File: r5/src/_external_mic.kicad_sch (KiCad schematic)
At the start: 139 parts, among them Q12 BSS84PW, Q13 BSS84PW, Q14 NX6008NBKW, Q15 NX3008NBKW, Q16 NX3008NBKW, Q17 NX3008NBKW, Q18 NX3008NBKW, Q19 NX3008NBKW, Q20 BSS84PW, Q21 BSS84PW, Q22 NX3008NBKW, Q23 NX3008NBKW, Q24 NX3008NBKW, Q25 Si2323DS, Q29 Si2323DS, Q30 NX3008NBKW, T18 , T19 , T20 , T23 , T24 , T25 , T26 , T27 , T28 , T29 , T30 , T31 , T32 , T33 , T34 , T35 , T37 , T38 , T43 , T44 , T45 , T46 , T47 , T48 , T49 , T50 , T59 , U17 74HC20, U18 THAT5173, U19 74HC74, U20 74HC132, U21 74HC4520, U22 74HC132, U23 THAT1580, U24 74HC688, U25 LM4562, U26 74HC688, U27 AD4005, U36 APX809S-40SA

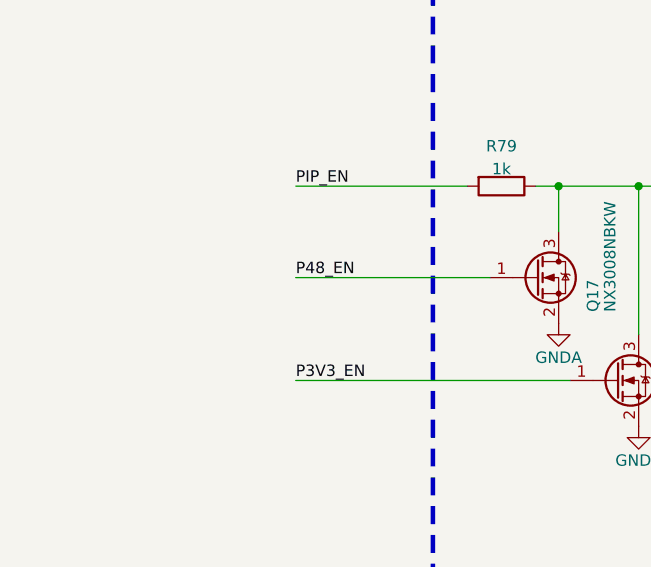
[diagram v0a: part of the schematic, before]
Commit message: Reestablish GND routing around amp control IC
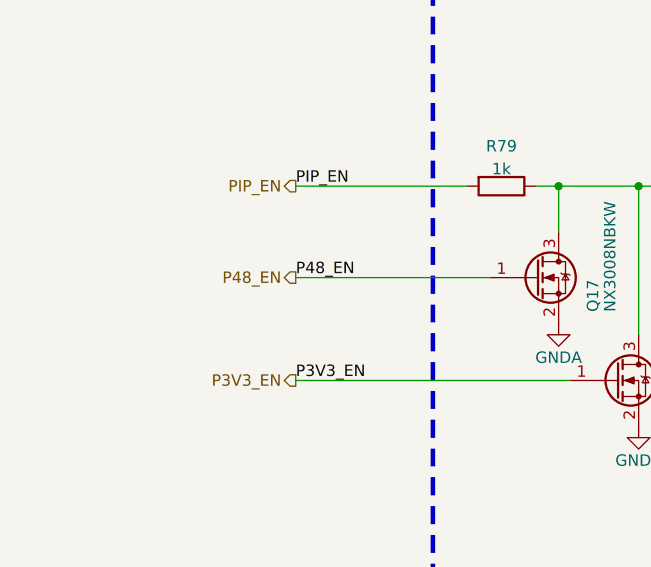
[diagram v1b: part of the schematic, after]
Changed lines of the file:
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@@
     (effects (font (size 1.27 1.27)) (justify left bottom))
+  )
+  (hierarchical_label "PIP_EN" (shape output) (at 53.34 234.95 180) (fields_autoplaced)
+    (effects (font (size 1.27 1.27)) (justify right))
   )
   (hierarchical_label "AMP_nCS" (shape input) (at 142.24 134.62 180) (fields_autoplaced)
@@
   )
   (hierarchical_label "MIC_IN_P" (shape input) (at 92.71 330.2 180) (fields_autoplaced)
+    (effects (font (size 1.27 1.27)) (justify right))
+  )
+  (hierarchical_label "P3V3_EN" (shape output) (at 53.34 256.54 180) (fields_autoplaced)
     (effects (font (size 1.27 1.27)) (justify right))
   )
@@
     (effects (font (size 1.27 1.27)) (justify right))
   )
+  (hierarchical_label "P48_EN" (shape output) (at 53.34 245.11 180) (fields_autoplaced)
+    (effects (font (size 1.27 1.27)) (justify right))
+  )

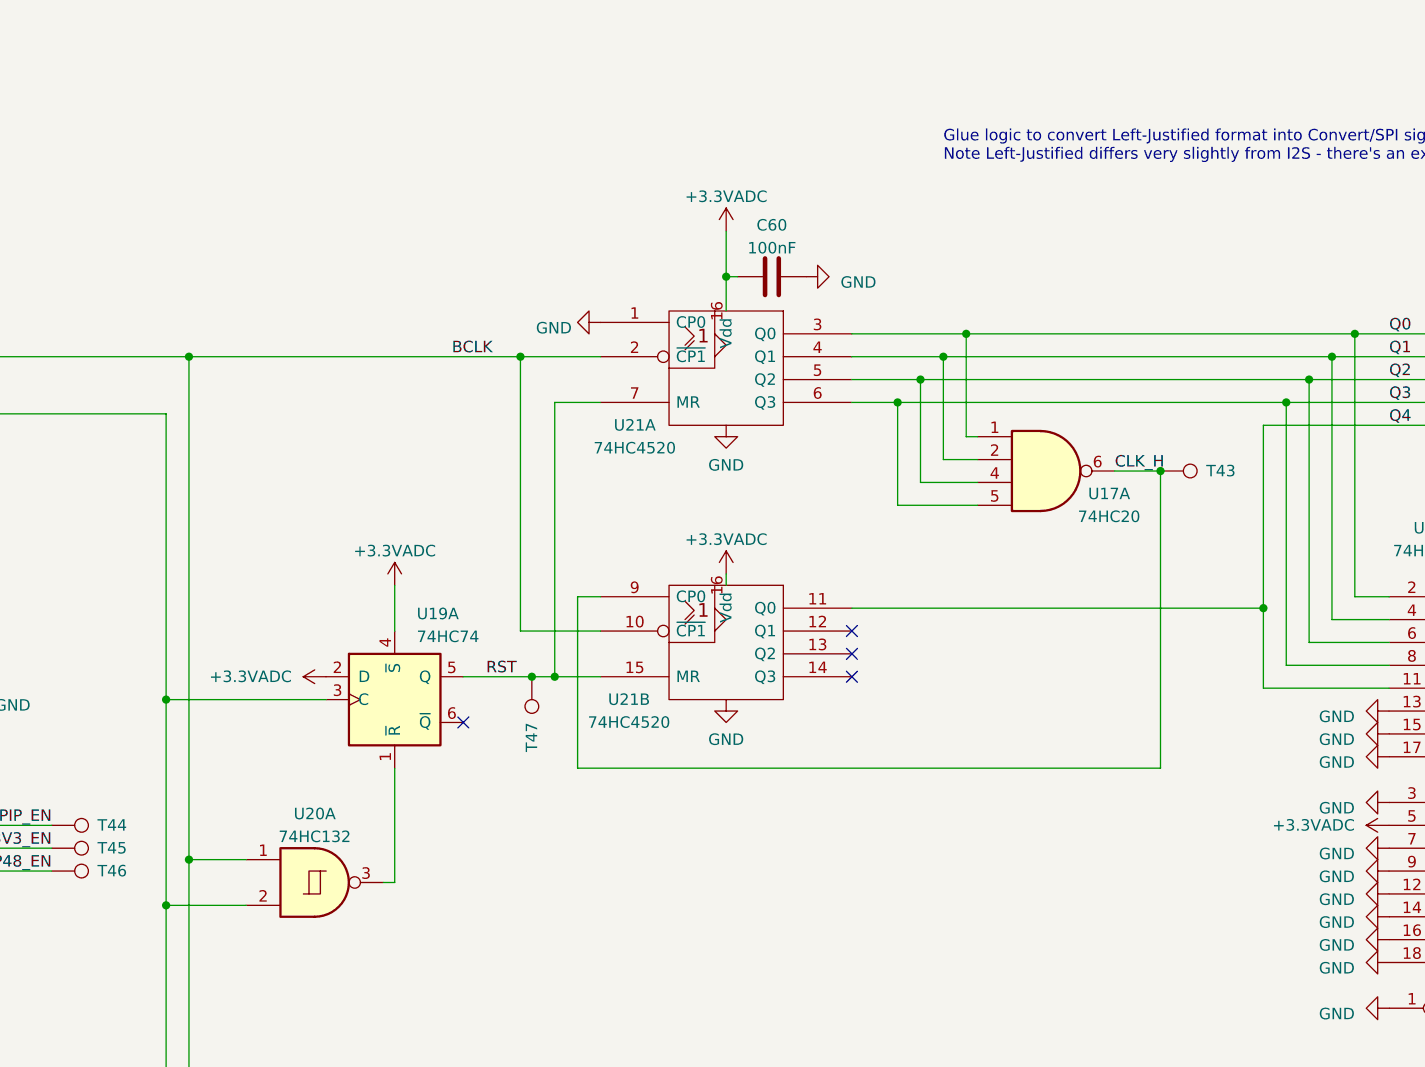
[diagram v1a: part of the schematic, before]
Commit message: Update schematic to include the latest library symbols. Mainly this updated the symbol fields, but three symbols actually changed, which required schematic edits to reconnect their pins. No circuit changes were made, and this was verified by checking the preview data in the PCB's "Update PCB from Schematic..." dialog.
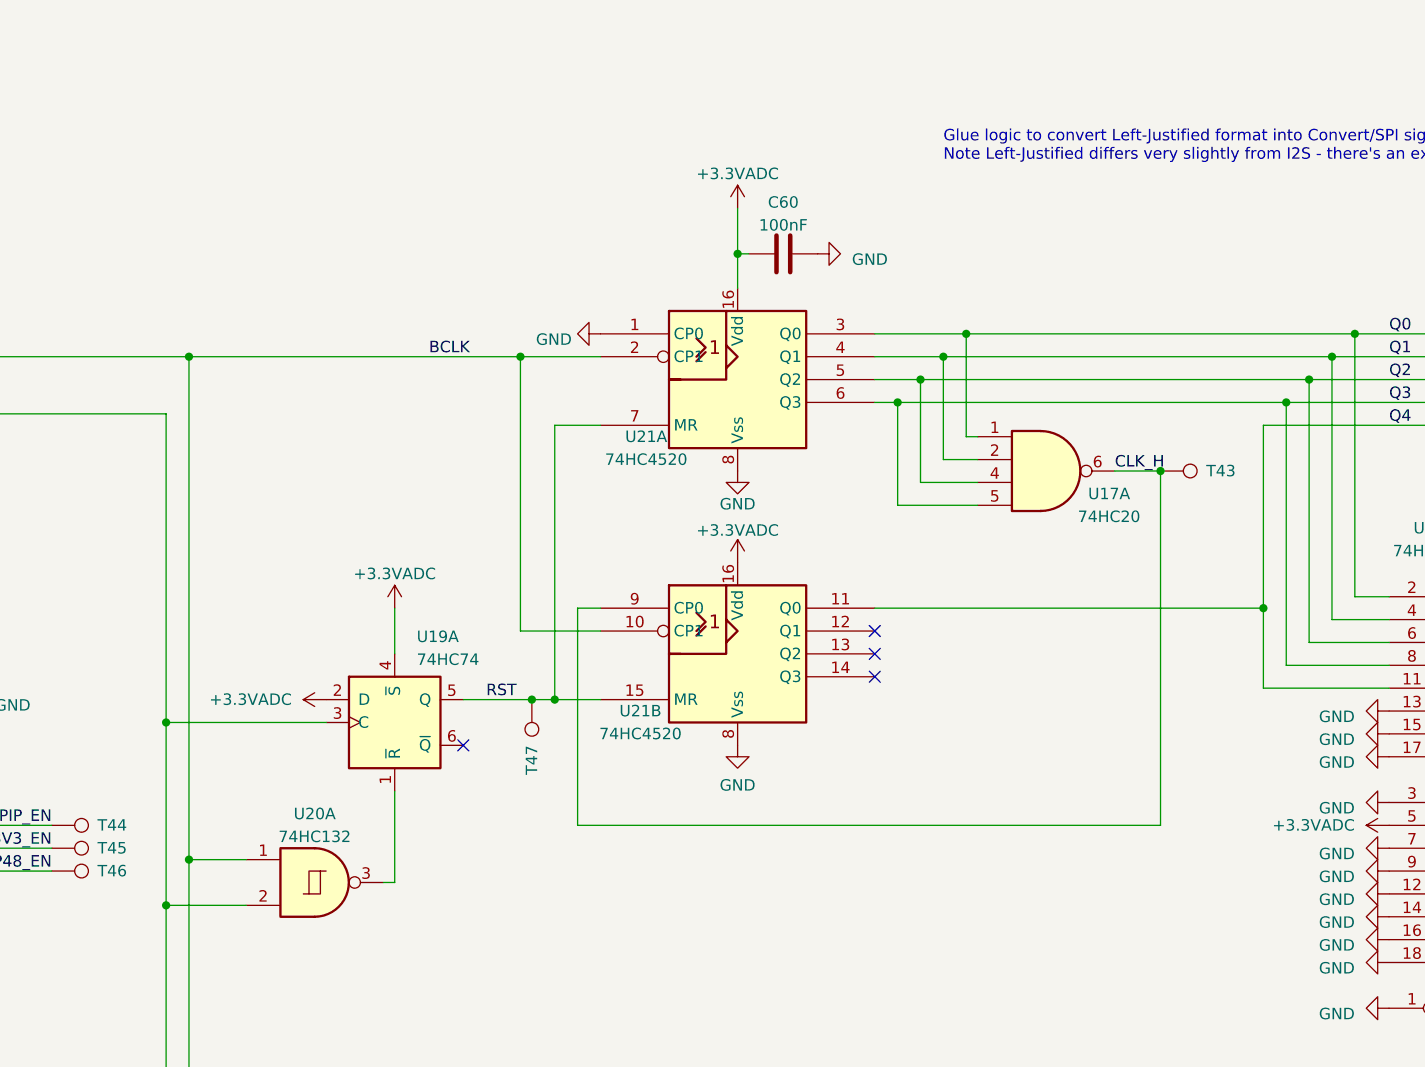
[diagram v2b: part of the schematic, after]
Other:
- moved on the sheet: C60, T47, U19A

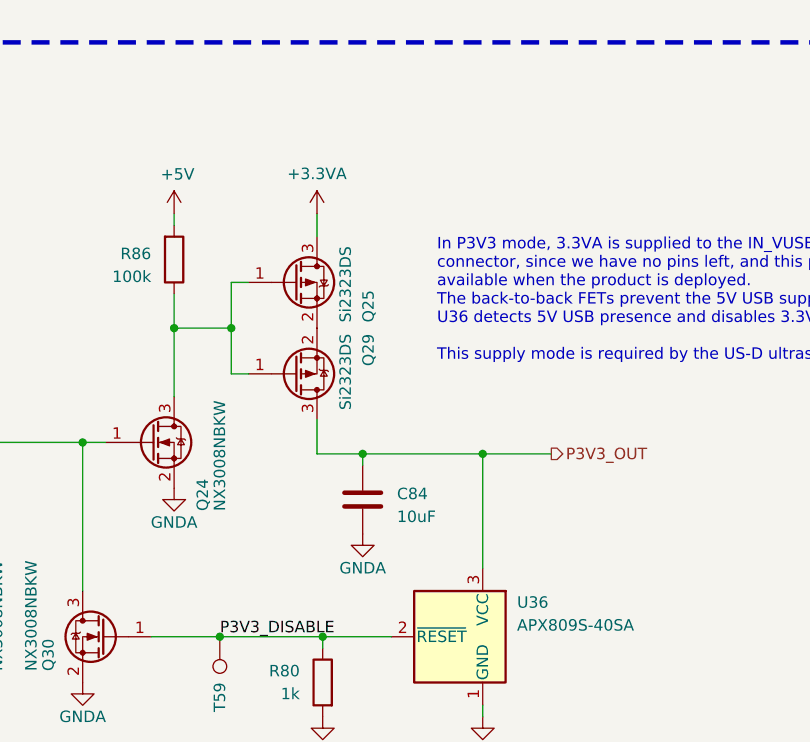
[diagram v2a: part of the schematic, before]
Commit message: Just realised I forgot to run the ERC. Added various PWR_FLAGs, corrected off-grid parts, etc. Updated board - no electrical changes.
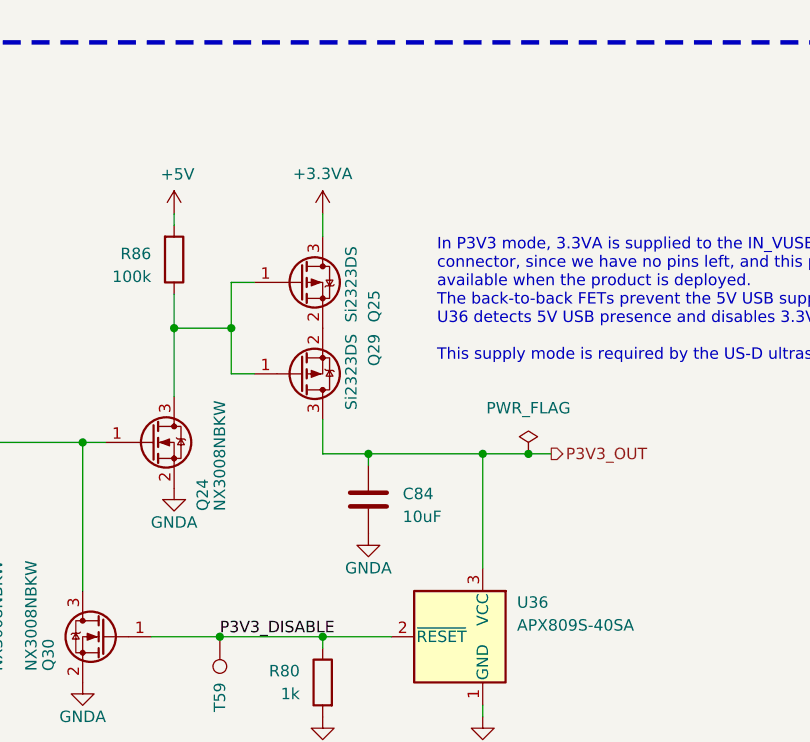
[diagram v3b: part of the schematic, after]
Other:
- moved on the sheet: C84, Q25, Q29
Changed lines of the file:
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@@
   (junction (at 227.33 133.35) (diameter 0) (color 0 0 0 0)
   )
-  (junction (at 306.705 236.22) (diameter 0) (color 0 0 0 0)
+  (junction (at 325.12 236.22) (diameter 0) (color 0 0 0 0)
+  )
+  (junction (at 307.34 236.22) (diameter 0) (color 0 0 0 0)
   )
   (junction (at 172.72 36.83) (diameter 0) (color 0 0 0 0)
@@
     (stroke (width 0) (type default))
   )
-  (wire (pts (xy 292.1 227.33) (xy 294.005 227.33))
+  (wire (pts (xy 292.1 227.33) (xy 294.64 227.33))
     (stroke (width 0) (type default))
   )
@@
     (stroke (width 0) (type default))
   )
-  (wire (pts (xy 301.625 209.55) (xy 301.625 212.09))
+  (wire (pts (xy 302.26 209.55) (xy 302.26 212.09))
     (stroke (width 0) (type default))
   )
@@
     (stroke (width 0) (type default))
   )
-  (wire (pts (xy 306.705 236.22) (xy 320.04 236.22))
+  (wire (pts (xy 307.34 236.22) (xy 320.04 236.22))
     (stroke (width 0) (type default))
   )
@@
     (stroke (width 0) (type default))
   )
-  (wire (pts (xy 301.625 232.41) (xy 301.625 236.22))
+  (wire (pts (xy 302.26 232.41) (xy 302.26 236.22))
     (stroke (width 0) (type default))
   )
@@
     (stroke (width 0) (type default))
   )
-  (wire (pts (xy 306.705 236.22) (xy 306.705 237.49))
+  (wire (pts (xy 307.34 236.22) (xy 307.34 237.49))
     (stroke (width 0) (type default))
   )
@@
     (stroke (width 0) (type default))
   )
+  (wire (pts (xy 325.12 236.22) (xy 327.66 236.22))
+    (stroke (width 0) (type default))
+  )
   (wire (pts (xy 461.01 312.42) (xy 473.71 312.42))
     (stroke (width 0) (type default))
@@
     (stroke (width 0) (type default))
   )
-  (wire (pts (xy 301.625 236.22) (xy 306.705 236.22))
+  (wire (pts (xy 302.26 236.22) (xy 307.34 236.22))
     (stroke (width 0) (type default))
   )
@@
     (stroke (width 0) (type default))
   )
-  (wire (pts (xy 320.04 236.22) (xy 327.66 236.22))
+  (wire (pts (xy 320.04 236.22) (xy 325.12 236.22))
     (stroke (width 0) (type default))
   )
@@
     (stroke (width 0) (type default))
   )
-  (wire (pts (xy 294.005 217.17) (xy 292.1 217.17))
+  (wire (pts (xy 294.64 217.17) (xy 292.1 217.17))
     (stroke (width 0) (type default))
   )
@@
     )
   )
-  (symbol (lib_id "Device:Q_PMOS_GSD") (at 299.085 217.17 0) (unit 1)
+  (symbol (lib_id "Device:Q_PMOS_GSD") (at 299.72 217.17 0) (unit 1)
     (exclude_from_sim no) (in_bom yes) (on_board yes) (dnp no)
-    (property "Reference" "Q25" (at 307.34 221.615 90)
+    (property "Reference" "Q25" (at 307.975 221.615 90)
       (effects (font (size 1.27 1.27)) (justify left))
     )
-    (property "Value" "Si2323DS" (at 304.8 221.615 90)
+    (property "Value" "Si2323DS" (at 305.435 221.615 90)
       (effects (font (size 1.27 1.27)) (justify left))
     )
-    (property "Footprint" "Package_TO_SOT_SMD:SOT-23" (at 304.165 214.63 0)
+    (property "Footprint" "Package_TO_SOT_SMD:SOT-23" (at 304.8 214.63 0)
       (effects (font (size 1.27 1.27)) hide)
     )
-    (property "Datasheet" "~" (at 299.085 217.17 0)
+    (property "Datasheet" "~" (at 299.72 217.17 0)
       (effects (font (size 1.27 1.27)) hide)
     )
-    (property "Description" "" (at 299.085 217.17 0)
+    (property "Description" "" (at 299.72 217.17 0)
       (effects (font (size 1.27 1.27)) hide)
     )
@@
     )
   )
+  (symbol (lib_id "power:PWR_FLAG") (at 325.12 236.22 0) (unit 1)
+    (exclude_from_sim no) (in_bom yes) (on_board yes) (dnp no) (fields_autoplaced)
+    (property "Reference" "#FLG014" (at 325.12 234.315 0)
+      (effects (font (size 1.27 1.27)) hide)
+    )
+    (property "Value" "PWR_FLAG" (at 325.12 231.14 0)
+      (effects (font (size 1.27 1.27)))
+    )
+    (property "Footprint" "" (at 325.12 236.22 0)
+      (effects (font (size 1.27 1.27)) hide)
+    )
+    (property "Datasheet" "~" (at 325.12 236.22 0)
+      (effects (font (size 1.27 1.27)) hide)
+    )
+    (property "Description" "Special symbol for telling ERC where power comes from" (at 325.12 236.22 0)
+      (effects (font (size 1.27 1.27)) hide)
+    )
+    (pin "1")
+    (instances
+      (project "bugg-main-r5"
+        (path "/e3eb514f-6ce4-4abe-ba20-f82f0015628f/e93db74d-0429-4e7f-b256-c16b4c3a83e7"
+          (reference "#FLG014") (unit 1)
+        )
+        (path "/e3eb514f-6ce4-4abe-ba20-f82f0015628f/41f15edd-4583-4f5d-8a81-daeb7c83b416"
+          (reference "#FLG019") (unit 1)
+        )
+      )
+    )
+  )
   (symbol (lib_id "74xx:74LS132") (at 148.59 35.56 0) (unit 5)
     (exclude_from_sim no) (in_bom yes) (on_board yes) (dnp no) (fields_autoplaced)
@@
     )
   )
-  (symbol (lib_id "Device:C") (at 306.705 241.3 180) (unit 1)
+  (symbol (lib_id "Device:C") (at 307.34 241.3 180) (unit 1)
     (exclude_from_sim no) (in_bom yes) (on_board yes) (dnp no)
-    (property "Reference" "C84" (at 310.515 240.665 0)
+    (property "Reference" "C84" (at 311.15 240.665 0)
       (effects (font (size 1.27 1.27)) (justify right))
     )
-    (property "Value" "10uF" (at 310.515 243.205 0)
+    (property "Value" "10uF" (at 311.15 243.205 0)
       (effects (font (size 1.27 1.27)) (justify right))
     )
-    (property "Footprint" "Capacitor_SMD:C_0603_1608Metric" (at 305.7398 237.49 0)
+    (property "Footprint" "Capacitor_SMD:C_0603_1608Metric" (at 306.3748 237.49 0)
       (effects (font (size 1.27 1.27)) hide)
     )
-    (property "Datasheet" "~" (at 306.705 241.3 0)
+    (property "Datasheet" "~" (at 307.34 241.3 0)
       (effects (font (size 1.27 1.27)) hide)
     )
-    (property "Description" "" (at 306.705 241.3 0)
+    (property "Description" "" (at 307.34 241.3 0)
       (effects (font (size 1.27 1.27)) hide)
     )
-    (property "Voltage" "6.3V" (at 306.705 241.3 0)
+    (property "Voltage" "6.3V" (at 307.34 241.3 0)
       (effects (font (size 1.27 1.27)) hide)
     )
@@
     )
   )
-  (symbol (lib_id "power:GNDA") (at 306.705 245.11 0) (unit 1)
+  (symbol (lib_id "power:GNDA") (at 307.34 245.11 0) (unit 1)
     (exclude_from_sim no) (in_bom yes) (on_board yes) (dnp no)
-    (property "Reference" "#PWR0246" (at 306.705 251.46 0)
+    (property "Reference" "#PWR0246" (at 307.34 251.46 0)
       (effects (font (size 1.27 1.27)) hide)
     )
-    (property "Value" "GNDA" (at 306.705 248.92 0)
+    (property "Value" "GNDA" (at 307.34 248.92 0)
       (effects (font (size 1.27 1.27)))
     )
-    (property "Footprint" "" (at 306.705 245.11 0)
+    (property "Footprint" "" (at 307.34 245.11 0)
       (effects (font (size 1.27 1.27)) hide)
     )
-    (property "Datasheet" "" (at 306.705 245.11 0)
+    (property "Datasheet" "" (at 307.34 245.11 0)
       (effects (font (size 1.27 1.27)) hide)
     )
-    (property "Description" "" (at 306.705 245.11 0)
+    (property "Description" "" (at 307.34 245.11 0)
       (effects (font (size 1.27 1.27)) hide)
     )
@@
     )
   )
-  (symbol (lib_id "Device:Q_PMOS_GSD") (at 299.085 227.33 0) (mirror x) (unit 1)
+  (symbol (lib_id "Device:Q_PMOS_GSD") (at 299.72 227.33 0) (mirror x) (unit 1)
     (exclude_from_sim no) (in_bom yes) (on_board yes) (dnp no)
-    (property "Reference" "Q29" (at 307.34 222.885 90)
+    (property "Reference" "Q29" (at 307.975 222.885 90)
       (effects (font (size 1.27 1.27)) (justify left))
     )
-    (property "Value" "Si2323DS" (at 304.8 222.885 90)
+    (property "Value" "Si2323DS" (at 305.435 222.885 90)
       (effects (font (size 1.27 1.27)) (justify left))
     )
-    (property "Footprint" "Package_TO_SOT_SMD:SOT-23" (at 304.165 229.87 0)
+    (property "Footprint" "Package_TO_SOT_SMD:SOT-23" (at 304.8 229.87 0)
       (effects (font (size 1.27 1.27)) hide)
     )
-    (property "Datasheet" "~" (at 299.085 227.33 0)
+    (property "Datasheet" "~" (at 299.72 227.33 0)
       (effects (font (size 1.27 1.27)) hide)
     )
-    (property "Description" "" (at 299.085 227.33 0)
+    (property "Description" "" (at 299.72 227.33 0)
       (effects (font (size 1.27 1.27)) hide)
     )
@@
     )
   )
-  (symbol (lib_id "power:+3.3VA") (at 301.625 209.55 0) (unit 1)
+  (symbol (lib_id "power:+3.3VA") (at 302.26 209.55 0) (unit 1)
     (exclude_from_sim no) (in_bom yes) (on_board yes) (dnp no)
-    (property "Reference" "#PWR0243" (at 301.625 213.36 0)
+    (property "Reference" "#PWR0243" (at 302.26 213.36 0)
       (effects (font (size 1.27 1.27)) hide)
     )
-    (property "Value" "+3.3VA" (at 301.625 205.105 0)
+    (property "Value" "+3.3VA" (at 302.26 205.105 0)
       (effects (font (size 1.27 1.27)))
     )
-    (property "Footprint" "" (at 301.625 209.55 0)
+    (property "Footprint" "" (at 302.26 209.55 0)
       (effects (font (size 1.27 1.27)) hide)
     )
-    (property "Datasheet" "" (at 301.625 209.55 0)
+    (property "Datasheet" "" (at 302.26 209.55 0)
       (effects (font (size 1.27 1.27)) hide)
     )
-    (property "Description" "" (at 301.625 209.55 0)
+    (property "Description" "" (at 302.26 209.55 0)
       (effects (font (size 1.27 1.27)) hide)
     )

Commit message: Rename Manufacturer field
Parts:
- T32, T33: now left out of the parts list
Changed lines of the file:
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@@
   )
   (symbol (lib_id "Connector:TestPoint") (at 473.71 330.2 180) (unit 1)
-    (exclude_from_sim no) (in_bom yes) (on_board yes) (dnp no)
+    (exclude_from_sim no) (in_bom no) (on_board yes) (dnp no)
     (property "Reference" "T33" (at 473.71 335.28 90)
       (effects (font (size 1.27 1.27)) (justify left))
@@
   )
   (symbol (lib_id "Connector:TestPoint") (at 473.71 312.42 0) (unit 1)
-    (exclude_from_sim no) (in_bom yes) (on_board yes) (dnp no)
+    (exclude_from_sim no) (in_bom no) (on_board yes) (dnp no)
     (property "Reference" "T32" (at 473.71 307.34 90)
       (effects (font (size 1.27 1.27)) (justify left))

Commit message: Change 0805 47uF to 1206 to save a BOM line. Update layout, DRC pass.
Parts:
- C25, C48, C52, C53, C57, C60, C63, C64, C65, C66, C67, C68, C69, C70, C74, C78, C79, C81: MPN (none) -> GRM155R71H104KE14D; Manufacturer (none) -> Murata; Mouser (none) -> 81-GRM155R71H104KE4D; Voltage (none) -> 50V
- C58, C59: MPN (none) -> 865250642008; Manufacturer (none) -> Wurth; Mouser (none) -> 710-865250642008
- C62: MPN (none) -> GRM155R71H104KE14D; Manufacturer (none) -> Murata; Mouser (none) -> 81-GRM155R71H104KE4D
